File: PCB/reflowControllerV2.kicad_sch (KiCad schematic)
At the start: 100 parts, among them J1 CN4, J10 NEXTION_OB, J11 PWR, J12 A-1JB, J2 SSR2, J3 SSR1, J4 FAN1, J5 FAN2, J6 T1, J7 T2, J8 SWD, J9 NEXTION_FRONT, Q1 2N3904, Q2 2N3904, Q3 2N3904, Q4 2N3904, Q5 2N3904, SW1 B3F-4055, U1 918-468K2029E50001, U10 ZD24C128A, U2 918-468K2029E50001, U3 AMS1117-3.3, U4 STM32WBxx_QFN48, U5 USBLC6-2SC6, U6 USBLC6-2SC6, U7 CH340G, U8 MAX31855KASA, U9 MAX31855KASA, Y1 NX2016_32MHz, Y2 NX2012_32K768Hz, Y3 12M

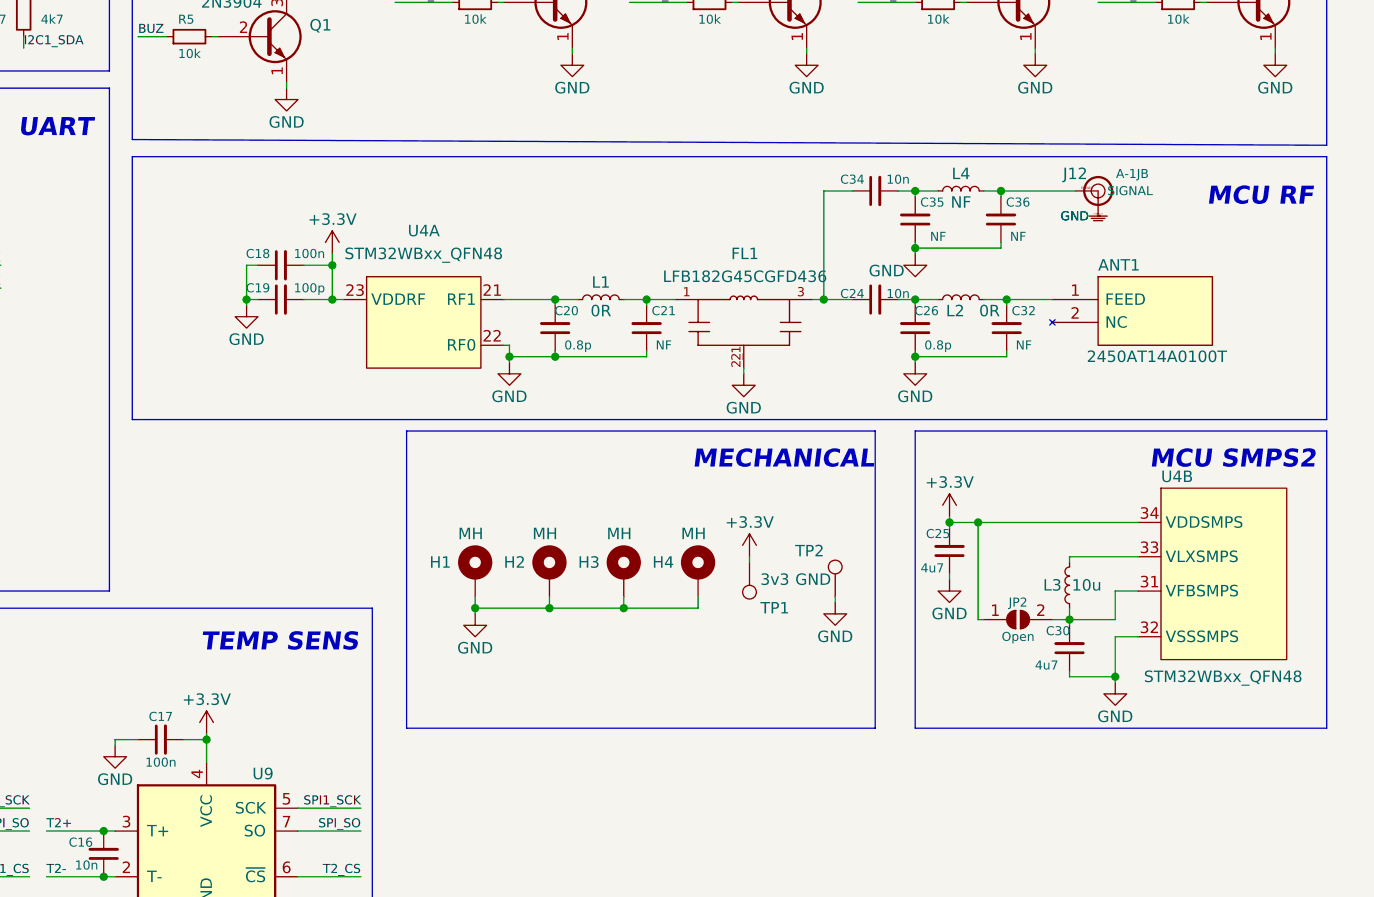
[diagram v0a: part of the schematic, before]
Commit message: PCB antenna removed
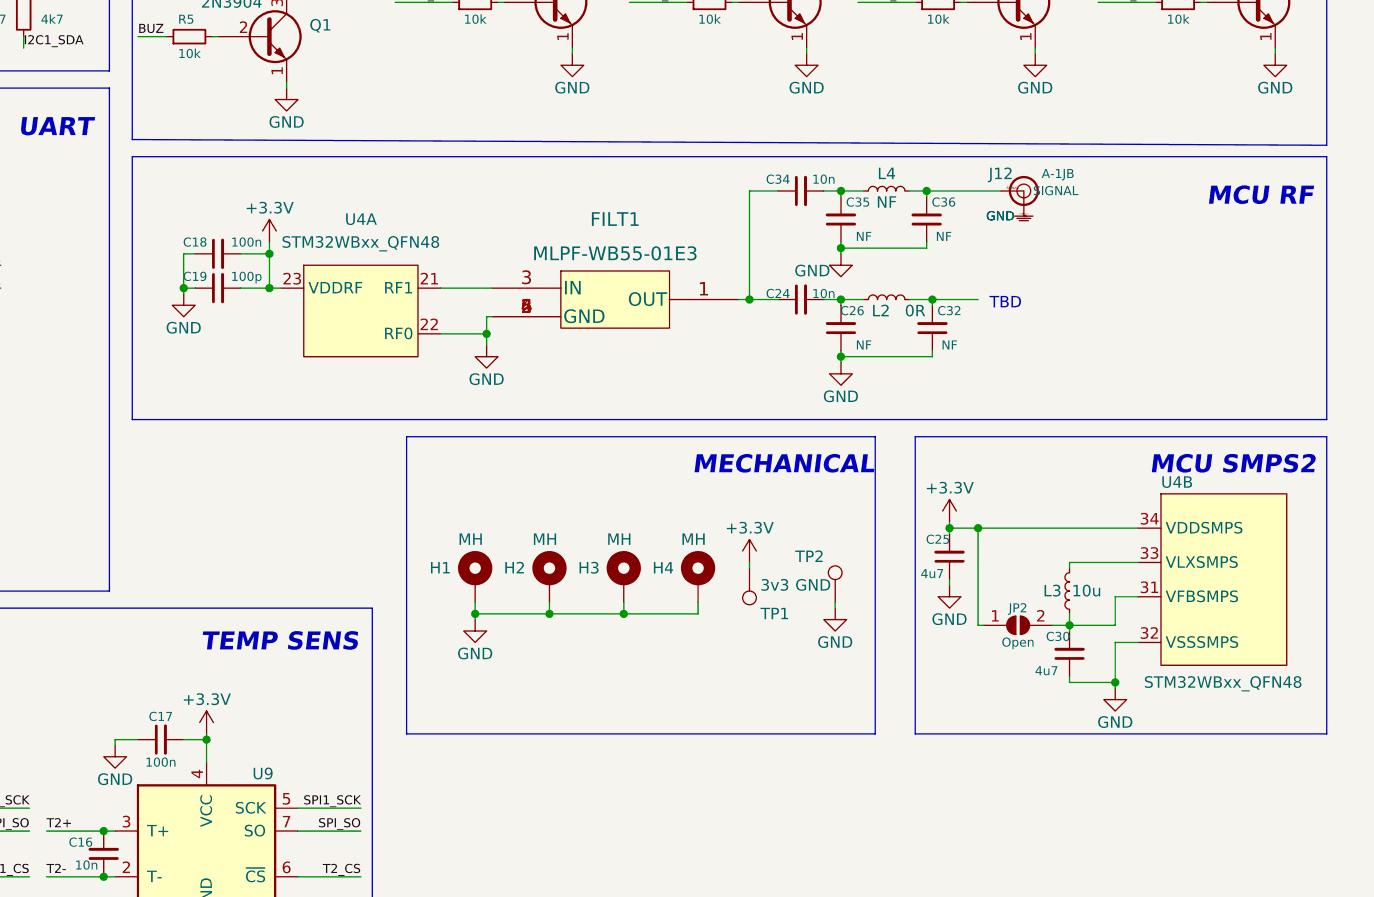
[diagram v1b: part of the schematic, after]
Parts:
- removed ANT1: 2450AT14A0100T, footprints:ANTC1608X40N, symbol MY_ANT:2450AT14A0100T
- removed C20: 0.8p, Capacitor_SMD:C_0402_1005Metric, symbol Device:C_Small
- removed C21: NF, Capacitor_SMD:C_0402_1005Metric, symbol Device:C_Small
- removed FL1: LFB182G45CGFD436, footprints:FIL_LFB182G45CGFD436, symbol MY_FILTER:LFB182G45CGFD436
- removed L1: 0R, Inductor_SMD:L_0402_1005Metric, symbol Device:L_Small
- added FILT1: MLPF-WB55-01E3, footprints:MLPF-WB55-01E3, symbol MY_RF:MLPF-WB55-01E3
- C26: value 0.8p -> NF
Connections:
- net GND: now also FILT1.2 (GND), FILT1.4 (GND), FILT1.5 (GND), FILT1.6 (GND)
- net at U4.21 (RF1): now also FILT1.3 (IN)
- net at C24.1, C34.1: now also FILT1.1 (OUT)
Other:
- note added: "TBD"
- moved on the sheet: C18, C19, C24, C25, C26, C30, C32, C34, C35, C36, H1, H2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

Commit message: Further component placing
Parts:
- added ANT1: M830520, footprints:M830520, symbol MY_RF:M830520
- J1: footprint Connector_PinHeader_2.54mm:PinHeader_1x04_P2.54mm_Vertical -> Connector_PinHeader_1.00mm:PinHeader_1x04_P1.00mm_Vertical
- JP1, JP2: footprint Jumper:SolderJumper-2_P1.3mm_Open_TrianglePad1.0x1.5mm -> Resistor_SMD:R_0603_1608Metric
- Y1: footprint Crystal:Crystal_SMD_3225-4Pin_3.2x2.5mm -> Crystal:Crystal_SMD_2016-4Pin_2.0x1.6mm
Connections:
- net GND: now also ANT1.3 (DP1), ANT1.4 (DP2), ANT1.5 (DP3), ANT1.6 (DP4)
- net T1+: now also J6.2 (Pin_2); no longer J6.1 (Pin_1)
- net T1-: now also J6.1 (Pin_1); no longer J6.2 (Pin_2)
- net T2+: now also J7.2 (Pin_2); no longer J7.1 (Pin_1)
- net T2-: now also J7.1 (Pin_1); no longer J7.2 (Pin_2)
- net at C32.2, L2.2: now also ANT1.1 (FEED), ANT1.2 (GND)
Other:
- note removed: "TBD"

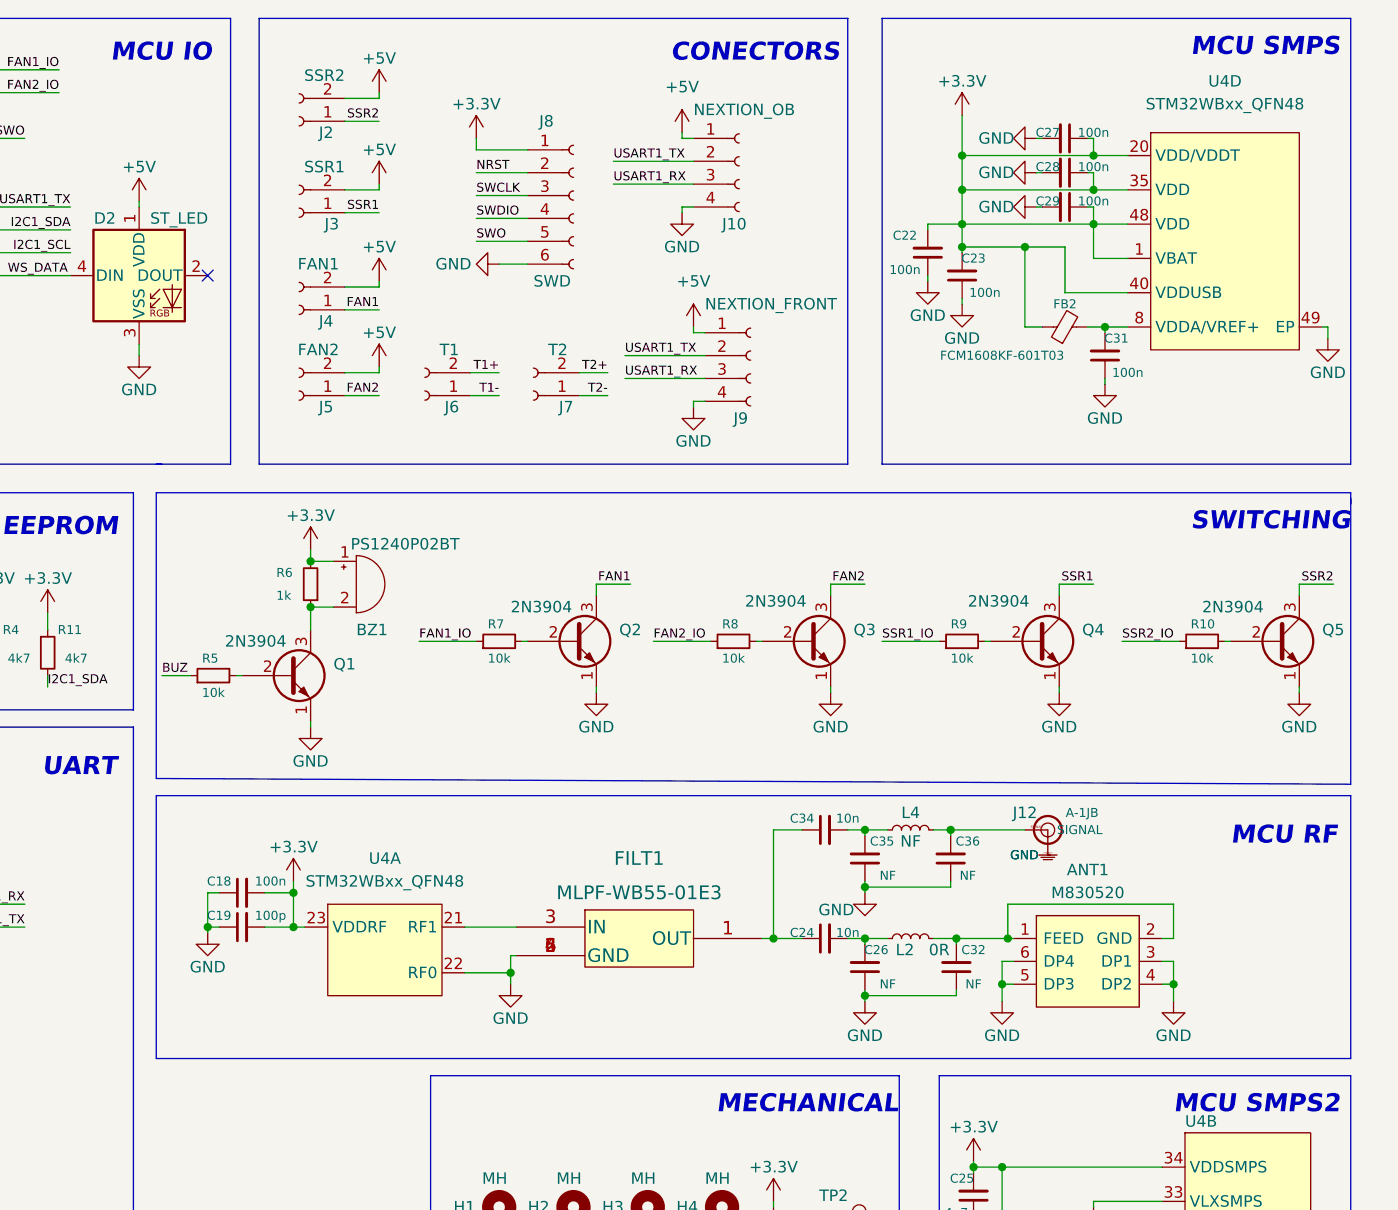
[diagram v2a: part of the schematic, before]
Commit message: RF Routing, Guard Ring, component placing, switching to mosfets
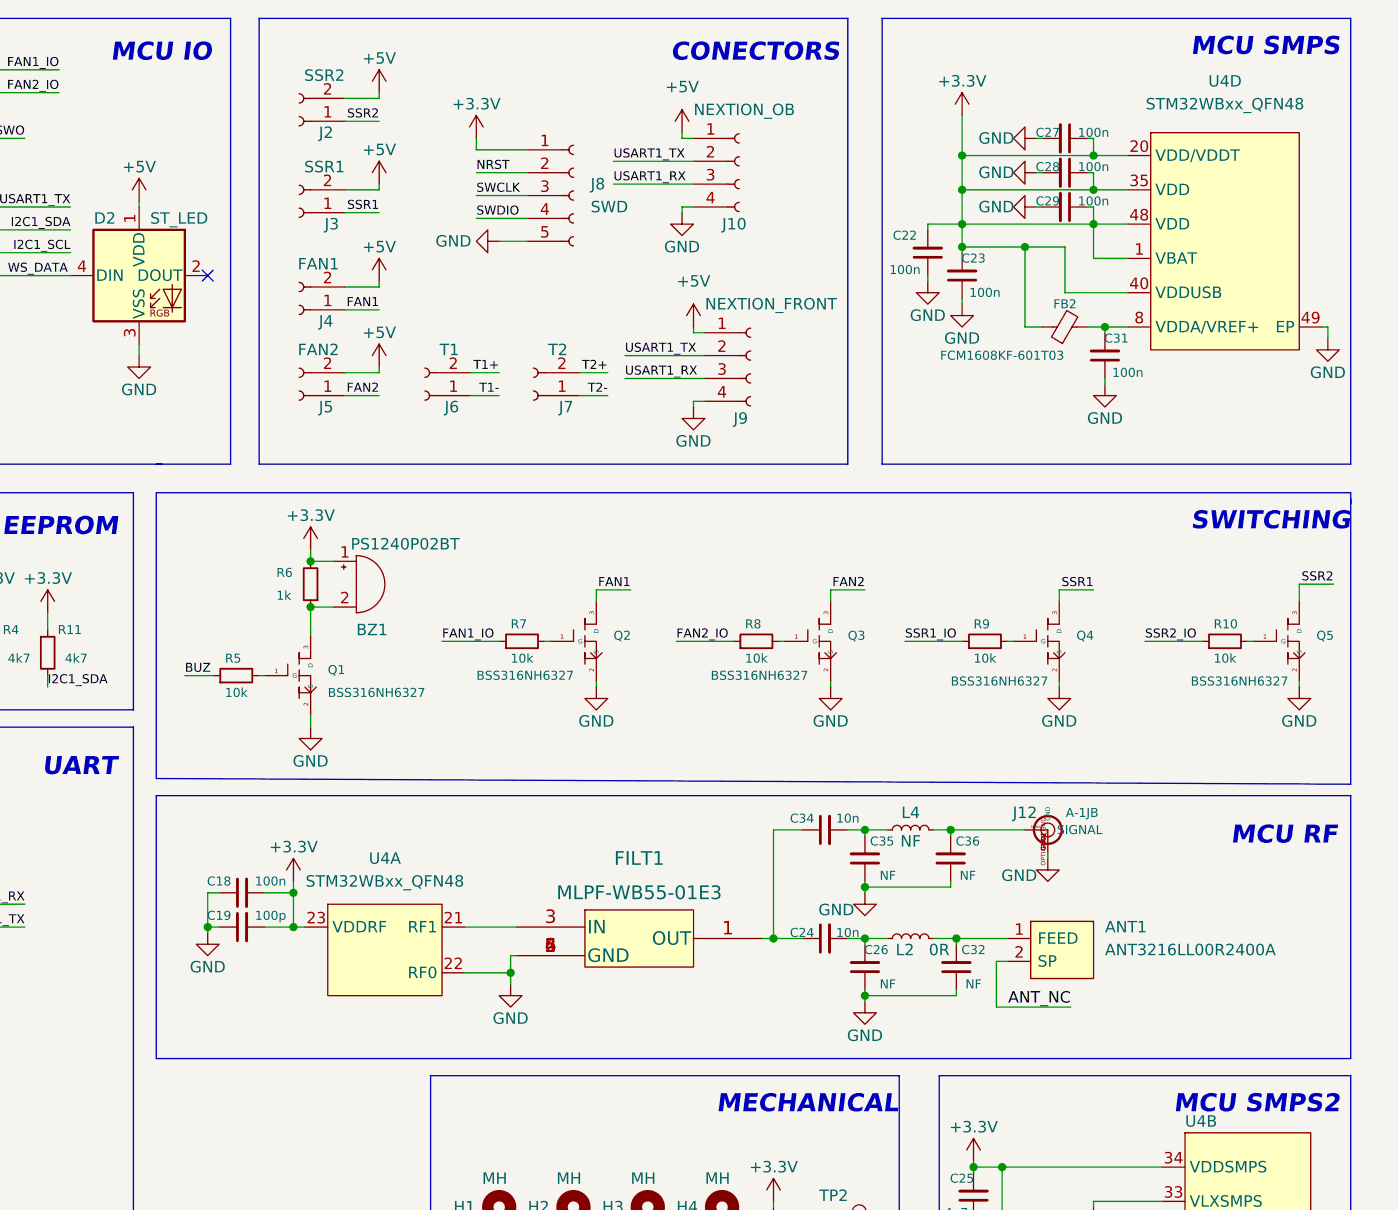
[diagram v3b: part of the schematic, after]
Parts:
- removed ANT1: M830520, footprints:M830520, symbol MY_RF:M830520
- removed J8: SWD, Connector_JST:JST_XH_B6B-XH-A_1x06_P2.50mm_Vertical, symbol Connector:Conn_01x06_Female
- removed Q1, Q2, Q3, Q4, Q5: 2N3904, Package_TO_SOT_THT:TO-92_Inline, symbol Transistor_BJT:2N3904
- added ANT1: ANT3216LL00R2400A, footprints:ANT3216LL00R2400A, symbol MY_RF:ANT3216LL00R2400A
- added J8: SWD, Connector_JST:JST_XH_B5B-XH-AM_1x05_P2.50mm_Vertical, symbol Connector:Conn_01x05_Female
- added Q1, Q2, Q3, Q4, Q5: BSS316NH6327, Package_TO_SOT_SMD:SOT-23, symbol rfcV2:BSS316NH6327
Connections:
- net +3V3: now also J8.1 (Pin_1)
- net FAN1: now also Q2.3 (D)
- net FAN2: now also Q3.3 (D)
- net GND: now also J12.GND1 (GND), J12.GND2 (GND), J12.OPTIONAL_GND (GND), J8.5 (Pin_5), Q1.2 (S), Q2.2 (S), Q3.2 (S), Q4.2 (S), Q5.2 (S)
- net NRST: now also J8.2 (Pin_2)
- net SSR1: now also Q4.3 (D)
- net SSR2: now also Q5.3 (D)
- net SWCLK: now also J8.3 (Pin_3)
- net SWDIO: now also J8.4 (Pin_4)
- net at R8.2: now also Q3.1 (G)
- net at C32.2, L2.2: now also ANT1.1 (FEED)
- net at BZ1.2 (+), R6.1: now also Q1.3 (D)
- net at R10.2: now also Q5.1 (G)
- net at R7.2: now also Q2.1 (G)
- net at R9.2: now also Q4.1 (G)
- net at R5.2: now also Q1.1 (G)
- new net ANT_NC: ANT1.2 (SP)
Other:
- moved on the sheet: R10, R5, R7, R8, R9

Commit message: Started layout, critical sections first
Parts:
- renumbered FILT1 to F1
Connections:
- net VIN: now reaches D3.2 (A), J11.2 (Pin_2)
- net 5V_IN: now reaches C3.2, C5.2, FB1.2, U3.3 (VI)
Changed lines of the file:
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@@
     (effects (font (size 1 1)) (justify right bottom))
   )
+  (label "5V_IN" (at 41.275 76.2 0)
+    (effects (font (size 1.27 1.27)) (justify left bottom))
+  )
   (label "LPUART1_RX" (at 92.71 26.67 0)
     (effects (font (size 1 1)) (justify left bottom))
@@
     (effects (font (size 1 1)) (justify left bottom))
   )
+  (label "VIN" (at 22.86 76.2 0)
+    (effects (font (size 1.27 1.27)) (justify left bottom))
+  )
   (label "SWDIO" (at 184.15 35.56 0)
     (effects (font (size 1 1)) (justify left bottom))
@@
   (symbol (lib_id "MY_RF:MLPF-WB55-01E3") (at 201.93 115.57 0) (unit 1)
     (in_bom yes) (on_board yes) (fields_autoplaced)
-    (property "Reference" "FILT1" (id 0) (at 202.2475 106.68 0)
+    (property "Reference" "F1" (id 0) (at 202.2475 106.68 0)
       (effects (font (size 1.524 1.524)))
     )
@@
       (effects (font (size 1 1)))
     )
-    (property "Value" "100O@100M" (id 1) (at 43.18 74.295 90)
+    (property "Value" "100O@100M" (id 1) (at 38.735 73.025 90)
       (effects (font (size 1 1)))
     )
@@
       (reference "D3") (unit 1) (value "PSBD1DF40V1H") (footprint "Diode_SMD:D_SOD-123F")
     )
+    (path "/643f2197-ccbc-4f7b-901f-1f4a5e9d450f"
+      (reference "F1") (unit 1) (value "MLPF-WB55-01E3") (footprint "footprints:MLPF-WB55-01E3")
+    )
     (path "/770f6496-c0da-4632-90ab-b02a09611f0f"
       (reference "FB1") (unit 1) (value "100O@100M") (footprint "Inductor_SMD:L_0603_1608Metric")
@@
       (reference "FB2") (unit 1) (value "FCM1608KF-601T03") (footprint "Inductor_SMD:L_0603_1608Metric")
     )
-    (path "/643f2197-ccbc-4f7b-901f-1f4a5e9d450f"
-      (reference "FILT1") (unit 1) (value "MLPF-WB55-01E3") (footprint "footprints:MLPF-WB55-01E3")
-    )
     (path "/8585d589-12e2-4e89-8feb-f60295a7430c"

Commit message: Layout done, improovements needed
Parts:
- removed J1: CN4, Connector_PinHeader_1.00mm:PinHeader_1x04_P1.00mm_Vertical, symbol Connector:Conn_01x04_Female
- J10: footprint Connector_JST:JST_XH_S4B-XH-A-1_1x04_P2.50mm_Horizontal -> footprints:JST_254_4P_H
- J2, J3, J4, J5, J6, J7: footprint Connector_JST:JST_XH_B2B-XH-A_1x02_P2.50mm_Vertical -> footprints:JST_254_2P_V
- J8: footprint Connector_JST:JST_XH_B5B-XH-AM_1x05_P2.50mm_Vertical -> footprints:JST_254_5P_V
- J9: footprint Connector_JST:JST_XH_B4B-XH-A_1x04_P2.50mm_Vertical -> footprints:JST_254_4P_V
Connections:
- net SPI_SO is gone; now on net SPI1_MISO: U8.7 (SO), U9.7 (SO)
- net FAN1: now also J5.1 (Pin_1); no longer J4.1 (Pin_1)
- net FAN2: now also J4.1 (Pin_1); no longer J5.1 (Pin_1)
- net FAN2_IO: now also U4.6 (PB9); no longer U4.29 (PB1)
- net NRST: now also J8.4 (Pin_4); no longer J8.2 (Pin_2)
- net SWDIO: now also J8.2 (Pin_2); no longer J8.4 (Pin_4)
- net WS_DATA: now also U4.29 (PB1); no longer U4.6 (PB9)
- no-connect marks 18 -> 20
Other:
- moved on the sheet: D2
